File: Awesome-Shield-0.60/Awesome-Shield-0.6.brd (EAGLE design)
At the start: 51 x 55 mm, 23 parts, among them SW1 SPST_TACT-EVQQ2, SW2 DPDT, U1 LIGHTSENSORTEMT6000

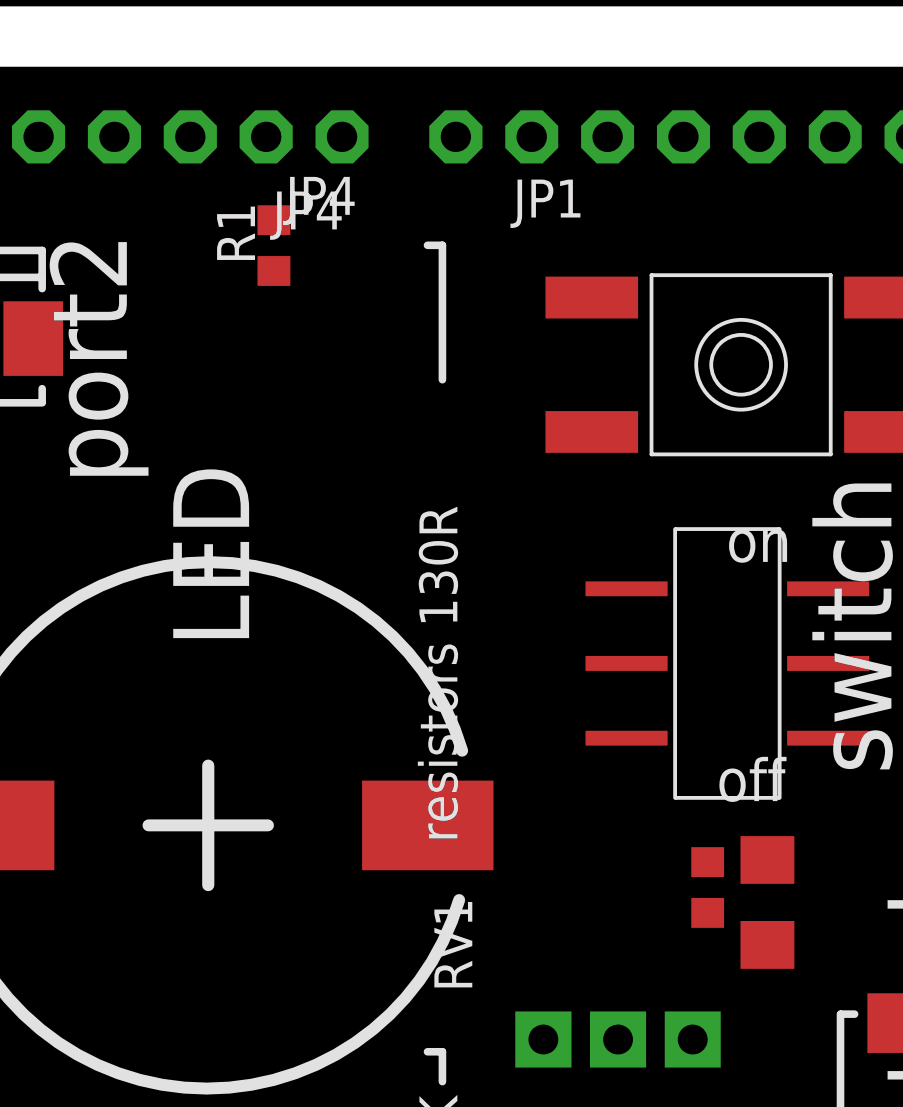
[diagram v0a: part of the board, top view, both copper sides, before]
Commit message: schematic cosmetics, change Rs to 1206 footprint
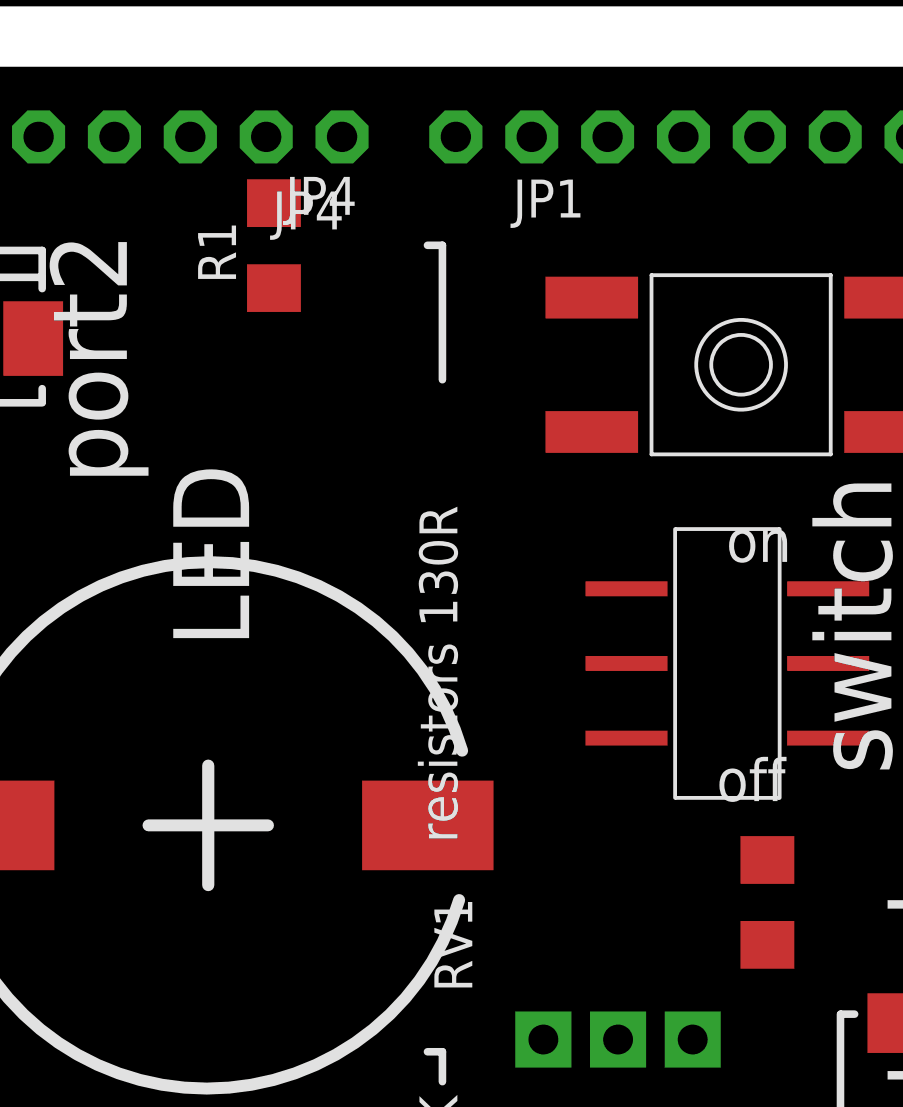
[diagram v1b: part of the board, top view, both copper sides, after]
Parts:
- removed R11: 10K, rcl:R0603
- R1: device rcl:R0603 -> rcl:R1206
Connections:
- net A1: no longer R11.2
- net GND: no longer R11.1
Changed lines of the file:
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@@
 <layer number="25" name="tNames" color="7" fill="1" visible="no" active="yes"/>
 <layer number="26" name="bNames" color="7" fill="1" visible="no" active="yes"/>
-<layer number="27" name="tValues" color="7" fill="1" visible="yes" active="yes"/>
+<layer number="27" name="tValues" color="7" fill="1" visible="no" active="yes"/>
 <layer number="28" name="bValues" color="7" fill="1" visible="no" active="yes"/>
 <layer number="29" name="tStop" color="7" fill="3" visible="no" active="yes"/>
 <layer number="30" name="bStop" color="7" fill="6" visible="no" active="yes"/>
-<layer number="31" name="tCream" color="7" fill="4" visible="yes" active="yes"/>
+<layer number="31" name="tCream" color="7" fill="4" visible="no" active="yes"/>
 <layer number="32" name="bCream" color="7" fill="5" visible="no" active="yes"/>
 <layer number="33" name="tFinish" color="6" fill="3" visible="no" active="yes"/>
@@
 <attribute name="PROD_ID" value="RES-09177" x="34.38" y="13.41" size="1.778" layer="27" rot="R90" display="off"/>
 </element>
-<element name="R11" library="rcl" package="R0603" value="10K" x="37.38" y="25.5" smashed="yes" rot="R90"/>
 <element name="J1" library="Seeed-OPL-Connector" package="HW4-SMD-2.0" value="" x="9.5" y="7" smashed="yes">
 <attribute name="VALUE" x="7.595" y="9.413" size="0.889" layer="27" font="vector" ratio="11"/>
@@
 </element>
 <element name="C1" library="rcl" package="C0603" value="100nF" x="5.08" y="33.02" rot="R90"/>
-<element name="R1" library="rcl" package="R0603" value="TBD" x="22.86" y="46.99" rot="R90"/>
+<element name="R1" library="rcl" package="R1206" value="TBD" x="22.86" y="46.99" rot="R90"/>
 </elements>
 <signals>
 <signal name="A1">
+<contactref element="JP3" pad="2"/>
 <contactref element="R6" pad="1"/>
-<contactref element="R11" pad="2"/>
 <contactref element="U1" pad="EMITTER"/>
-<contactref element="JP3" pad="2"/>
-<wire x1="39.38" y1="26.422" x2="37.38" y2="26.35" width="0" layer="19" extent="1-1"/>
-<wire x1="45.82" y1="26.03" x2="39.38" y2="26.422" width="0" layer="19" extent="1-1"/>
-<wire x1="36.56" y1="2.37" x2="45.82" y2="26.03" width="0" layer="19" extent="1-1"/>
+<wire x1="39.38" y1="26.422" x2="45.82" y2="26.03" width="0" layer="19" extent="1-1"/>
+<wire x1="36.56" y1="2.37" x2="39.38" y2="26.422" width="0" layer="19" extent="1-1"/>
 </signal>
 <signal name="GND">
 <contactref element="SW1" pad="A"/>
 <contactref element="SW1" pad="A'"/>
-<contactref element="SW2" pad="6"/>
-<contactref element="SW2" pad="3"/>
-<contactref element="SG1" pad="+"/>
 <polygon width="0.4064" layer="1" isolate="0.4064">
 <vertex x="47.8" y="53.1"/>
@@
 <contactref element="J2" pad="SS2"/>
 <contactref element="RV1" pad="P$1"/>
-<contactref element="R11" pad="1"/>
 <contactref element="R6" pad="2"/>
 <contactref element="JP2" pad="7"/>
@@
 <contactref element="C1" pad="2"/>
 <contactref element="D1" pad="3"/>
-<wire x1="33.5" y1="45.25" x2="43.5" y2="45.25" width="0" layer="19" extent="1-1"/>
-<wire x1="34.665" y1="35.5" x2="33.5" y2="45.25" width="0" layer="19" extent="1-1"/>
-<wire x1="41.415" y1="35.5" x2="34.665" y2="35.5" width="0" layer="19" extent="1-1"/>
-<wire x1="36.88" y1="20.41" x2="41.415" y2="35.5" width="0" layer="19" extent="1-1"/>
-<wire x1="37.38" y1="24.65" x2="36.88" y2="20.41" width="0" layer="19" extent="1-1"/>
-<wire x1="39.38" y1="23.578" x2="37.38" y2="24.65" width="0" layer="19" extent="1-1"/>
-<wire x1="15.3" y1="10.123" x2="39.38" y2="23.578" width="0" layer="19" extent="1-1"/>
-<wire x1="12.5" y1="7" x2="15.3" y2="10.123" width="0" layer="19" extent="1-1"/>
-<wire x1="3.7" y1="10.123" x2="12.5" y2="7" width="0" layer="19" extent="1-1"/>
-<wire x1="23.86" y1="2.37" x2="15.3" y2="10.123" width="0" layer="19" extent="1-1"/>
-<wire x1="26.4" y1="2.37" x2="23.86" y2="2.37" width="0" layer="19" extent="1-1"/>
-<wire x1="13.31" y1="27.58" x2="3.7" y2="10.123" width="0" layer="19" extent="1-1"/>
-<wire x1="43.977" y1="20.96" x2="12.5" y2="7" width="0" layer="19" extent="1-1"/>
+<contactref element="SG1" pad="+"/>
+<contactref element="SW2" pad="3"/>
+<contactref element="SW2" pad="6"/>
+<wire x1="41.415" y1="35.5" x2="43.5" y2="45.25" width="0" layer="19" extent="1-1"/>
+<wire x1="34.665" y1="35.5" x2="41.415" y2="35.5" width="0" layer="19" extent="1-1"/>
+<wire x1="33.5" y1="45.25" x2="34.665" y2="35.5" width="0" layer="19" extent="1-1"/>
+<wire x1="39.38" y1="23.578" x2="41.415" y2="35.5" width="0" layer="19" extent="1-1"/>
+<wire x1="36.88" y1="20.41" x2="39.38" y2="23.578" width="0" layer="19" extent="1-1"/>
+<wire x1="43.977" y1="20.96" x2="39.38" y2="23.578" width="0" layer="19" extent="1-1"/>
 <wire x1="47.1" y1="18.16" x2="43.977" y2="20.96" width="0" layer="19" extent="1-1"/>
-<wire x1="7.657" y1="26.34" x2="47.1" y2="18.16" width="0" layer="19" extent="1-1"/>
-<wire x1="5.08" y1="33.87" x2="7.657" y2="26.34" width="0" layer="19" extent="1-1"/>
 <wire x1="43.977" y1="9.36" x2="47.1" y2="18.16" width="0" layer="19" extent="1-1"/>
 <wire x1="14.8" y1="43.877" x2="33.5" y2="45.25" width="0" layer="19" extent="1-1"/>
@@
 <wire x1="6" y1="47" x2="9.9" y2="50.63" width="0" layer="19" extent="1-1"/>
 <wire x1="3.2" y1="43.877" x2="6" y2="47" width="0" layer="19" extent="1-1"/>
+<wire x1="5.08" y1="33.87" x2="3.2" y2="43.877" width="0" layer="19" extent="1-1"/>
+<wire x1="7.657" y1="26.34" x2="5.08" y2="33.87" width="0" layer="19" extent="1-1"/>
+<wire x1="13.31" y1="27.58" x2="7.657" y2="26.34" width="0" layer="19" extent="1-1"/>
+<wire x1="3.7" y1="10.123" x2="7.657" y2="26.34" width="0" layer="19" extent="1-1"/>
+<wire x1="12.5" y1="7" x2="3.7" y2="10.123" width="0" layer="19" extent="1-1"/>
+<wire x1="15.3" y1="10.123" x2="12.5" y2="7" width="0" layer="19" extent="1-1"/>
+<wire x1="23.86" y1="2.37" x2="15.3" y2="10.123" width="0" layer="19" extent="1-1"/>
+<wire x1="26.4" y1="2.37" x2="23.86" y2="2.37" width="0" layer="19" extent="1-1"/>
 </signal>
 <signal name="D2">
@@
 </signal>
 <signal name="D8">
+<contactref element="JP4" pad="1"/>
+<contactref element="SW2" pad="5"/>
 <contactref element="SW2" pad="2"/>
-<contactref element="SW2" pad="5"/>
-<contactref element="JP4" pad="1"/>
 <wire x1="34.665" y1="33" x2="25.14" y2="50.63" width="0" layer="19" extent="1-1"/>
 <wire x1="41.415" y1="33" x2="34.665" y2="33" width="0" layer="19" extent="1-1"/>
@@
 <contactref element="JP4" pad="2"/>
 <contactref element="R1" pad="2"/>
-<wire x1="22.86" y1="47.84" x2="22.6" y2="50.63" width="0" layer="19" extent="1-1"/>
+<wire x1="22.86" y1="48.412" x2="22.6" y2="50.63" width="0" layer="19" extent="1-1"/>
 </signal>
 <signal name="D4">
@@
 </signal>
 <signal name="N$2">
+<contactref element="R1" pad="1"/>
 <contactref element="SG1" pad="-"/>
-<contactref element="R1" pad="1"/>
-<wire x1="22.86" y1="46.14" x2="28.01" y2="27.58" width="0" layer="19" extent="1-1"/>
+<wire x1="28.01" y1="27.58" x2="22.86" y2="45.568" width="0" layer="19" extent="1-1"/>
 </signal>
 </signals>

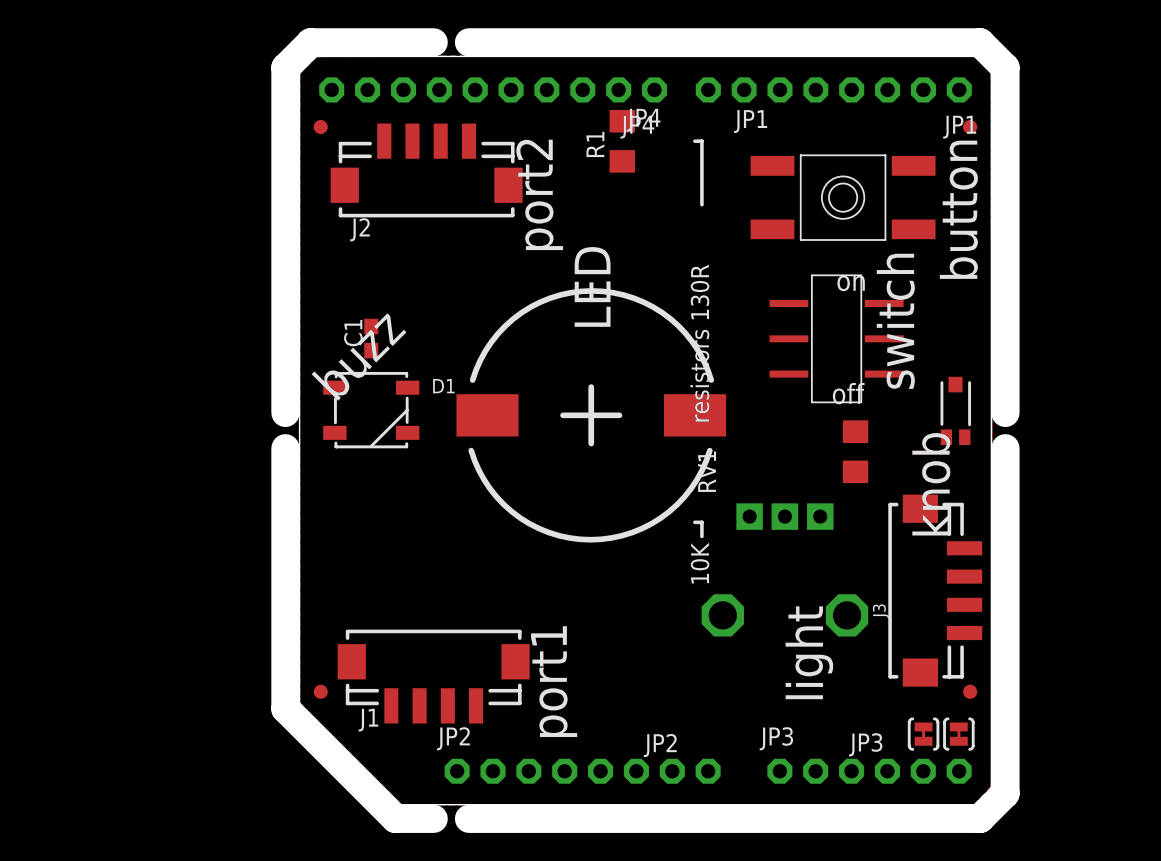
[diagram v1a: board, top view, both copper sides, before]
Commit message: change buzzer to Loudity t68-0808, sketch part
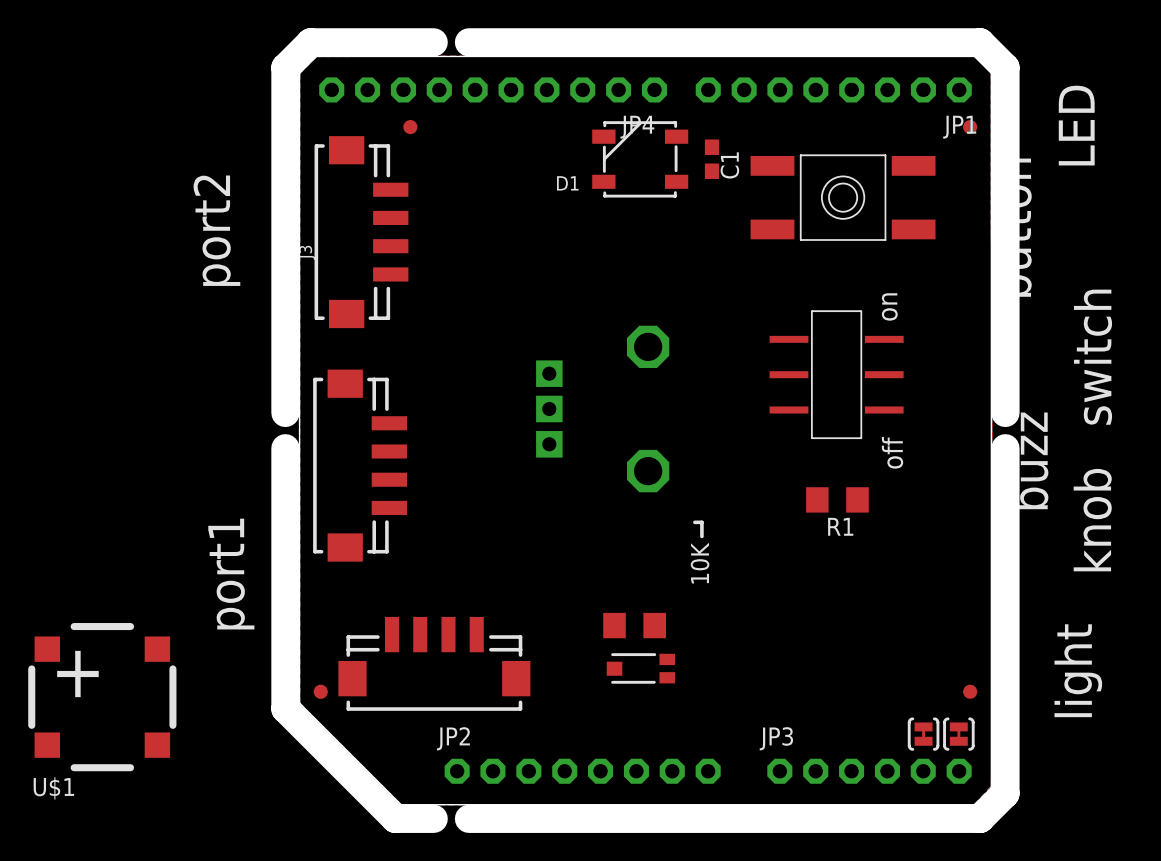
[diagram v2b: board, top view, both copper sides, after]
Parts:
- removed SG1: BUZZERSMD2, SparkFun-Electromechanical:BUZZER-CCV
- added U$1: LOUDITY-BZEL-T680808, buzzer-loudity-bzel-t68-0808:SMT-68
- moved J3 47.9 mm to (6.46, 40.6)
- moved R1 29.6 mm to (38.1, 21.6), turned to 180 degrees
- moved U1 28.8 mm to (24.2, 9.64), turned to 180 degrees
- moved C1 27.3 mm to (29.2, 45.7), turned to 270 degrees
- moved D1 26.1 mm to (24.1, 45.7), turned to 180 degrees
- moved J2 23.1 mm to (6.36, 24.0), turned to 90 degrees
- moved R6 19.9 mm to (23.7, 12.7), turned to 180 degrees
- moved RV1 17.5 mm to (24.7, 28.0), turned to 180 degrees
- moved FID4 6.35 mm to (7.85, 48.0)
- moved J1 5.05 mm to (9.55, 12.1), turned to 180 degrees
- moved SW2 2.54 mm to (38.0, 30.5)
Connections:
- net GND: now also U$1.GND; no longer SG1.+
- net N$2: now also U$1.SIG; no longer SG1.-
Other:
- board text removed: "J1"
- board text removed: "J2"
- board text removed: "JP1"
- board text removed: "JP2"
- board text removed: "JP3"
- board text removed: "JP4"
- board text removed: "RV1"
- board text removed: "resistors 130R"

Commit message: all components on imperial grid
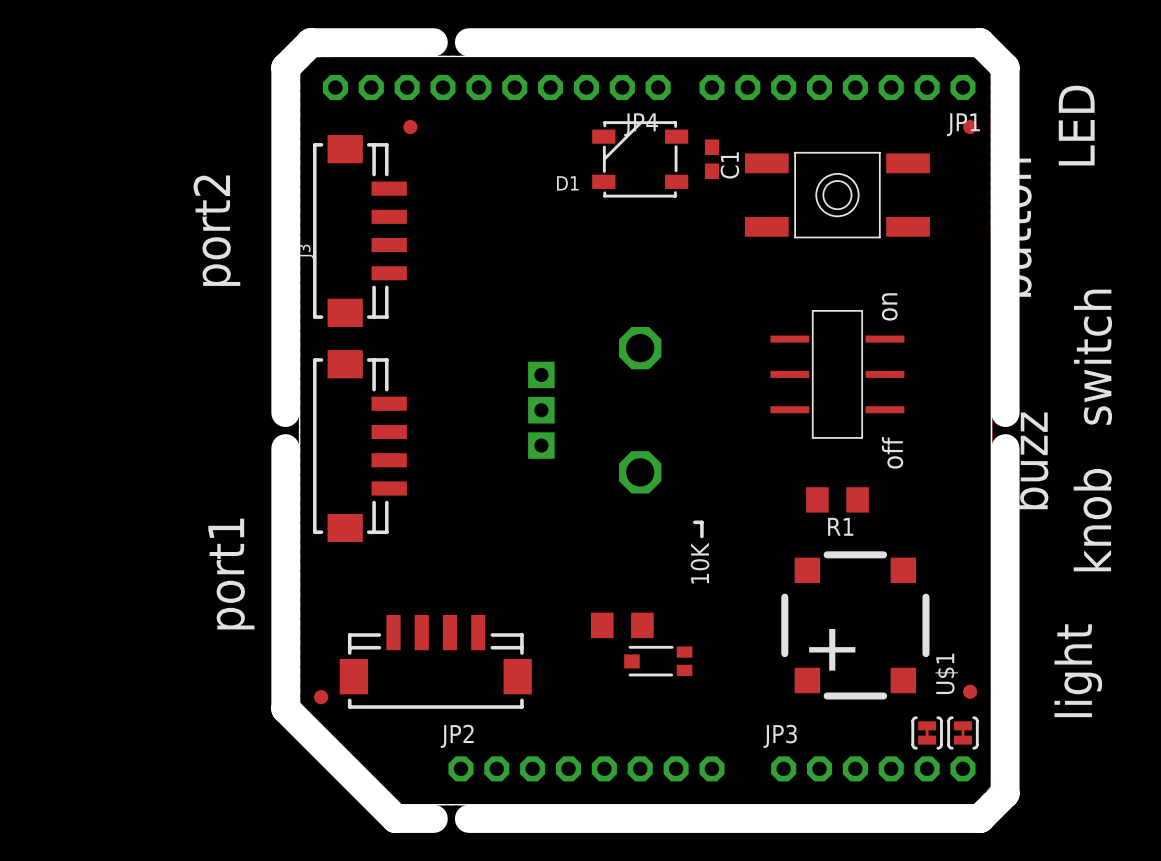
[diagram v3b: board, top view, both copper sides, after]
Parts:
- moved U$1 53.6 mm to (39.4, 12.7), turned to 90 degrees
- moved J2 1.38 mm to (6.35, 25.4)
- moved U1 1.34 mm to (25.4, 10.2)
- moved R6 0.87 mm to (22.9, 12.7)
- moved RV1 0.57 mm to (24.1, 27.9)
- moved SW1 0.44 mm to (38.1, 43.2)
- moved FID1 0.38 mm to (1.52, 7.62)
- moved JP3 0.32 mm to (40.6, 2.54)
- moved JP2 0.32 mm to (20.3, 2.54)
- moved JP4 0.31 mm to (14.0, 50.8)
- moved JP1 0.31 mm to (38.1, 50.8)
- moved SJ2 0.30 mm to (47.0, 5.08)
- moved SJ1 0.26 mm to (44.5, 5.08)
- moved J1 0.17 mm to (9.65, 12.2)
- moved J3 0.14 mm to (6.35, 40.6)
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
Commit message: LED data to D5 instead of D6
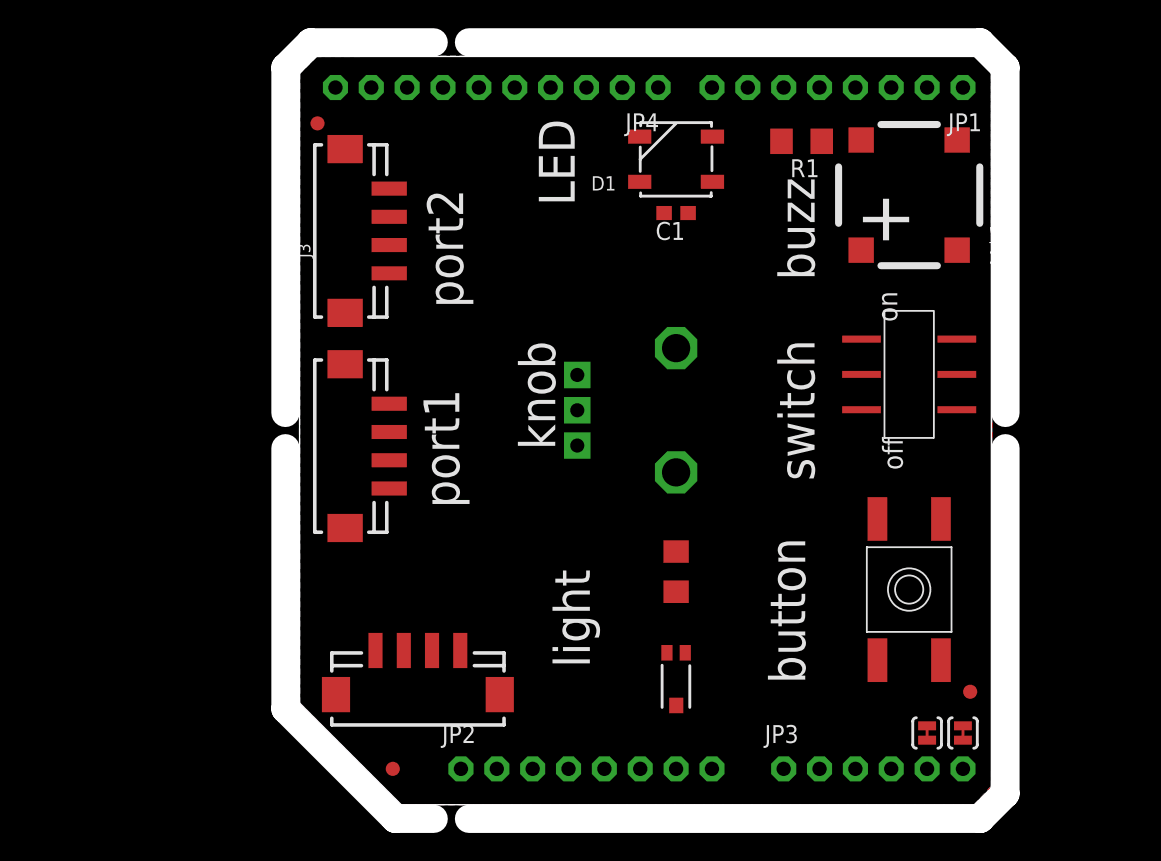
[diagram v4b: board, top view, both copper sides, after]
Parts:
- removed FID2: FIDUCIAL1X2, SparkFun-Aesthetics:FIDUCIAL-1X2
- moved U$1 30.7 mm to (43.2, 43.2)
- moved SW1 28.4 mm to (43.2, 15.2), turned to 270 degrees
- moved R1 25.5 mm to (35.6, 47.0)
- moved FID1 7.18 mm to (6.60, 2.54)
- moved FID4 6.59 mm to (1.27, 48.3)
- moved R6 5.39 mm to (26.7, 16.5), turned to 90 degrees
- moved SW2 5.08 mm to (43.2, 30.5)
- moved C1 4.58 mm to (26.7, 41.9), turned to 180 degrees
- moved D1 2.54 mm to (26.7, 45.7)
- moved RV1 2.54 mm to (26.7, 27.9)
- moved U1 1.80 mm to (26.7, 8.89), turned to 270 degrees
- moved J1 1.80 mm to (8.38, 10.9)
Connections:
- net D5: now also D1.4
- net D6: no longer D1.4
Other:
- board text removed: "10K"

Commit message: routing
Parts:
- J1: value (none) -> PORT1
- moved J2 2.54 mm to (6.35, 22.9)
- moved R6 1.27 mm to (26.7, 15.2)
- moved FID3 1.27 mm to (47.5, 9.27)
- moved U1 0.63 mm to (26.7, 8.26)
- moved C1 0.63 mm to (26.7, 41.3)
- moved D1 0.63 mm to (26.7, 45.1)
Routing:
- net SCL: track 0.00 -> 77.8 mm, vias 0 -> 2
- net SDA: track 0.00 -> 75.5 mm, vias 0 -> 2
- net A2: track 0.00 -> 68.7 mm
- net D4: track 0.00 -> 61.3 mm, vias 0 -> 1
- net A0: track 0.00 -> 50.4 mm, vias 0 -> 1
- net D2: track 0.00 -> 47.1 mm, vias 0 -> 1
- net A3: track 0.00 -> 45.6 mm, vias 0 -> 1
- net IOREF: track 0.00 -> 39.8 mm
- net D8: track 0.00 -> 38.5 mm
- net D6: track 0.00 -> 36.4 mm, vias 0 -> 1
- net A1: track 0.00 -> 19.6 mm
- net D5: track 0.00 -> 16.2 mm, vias 0 -> 1
- net D9: track 0.00 -> 12.9 mm
- net N$2: track 0.00 -> 9.19 mm
- net +5V: track 0.00 -> 3.54 mm
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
